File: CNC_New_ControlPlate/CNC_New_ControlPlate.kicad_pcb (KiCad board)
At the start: 2 copper layers, 152 x 73 mm, 38 parts, among them J1 OTHER, J2 Conn_01x02, J3 STEPPERS, J4 SPINDEL, U1 PC847, U2 PC847, U3 7406, U4 ATtiny2313V-10P, Y1 4MHz

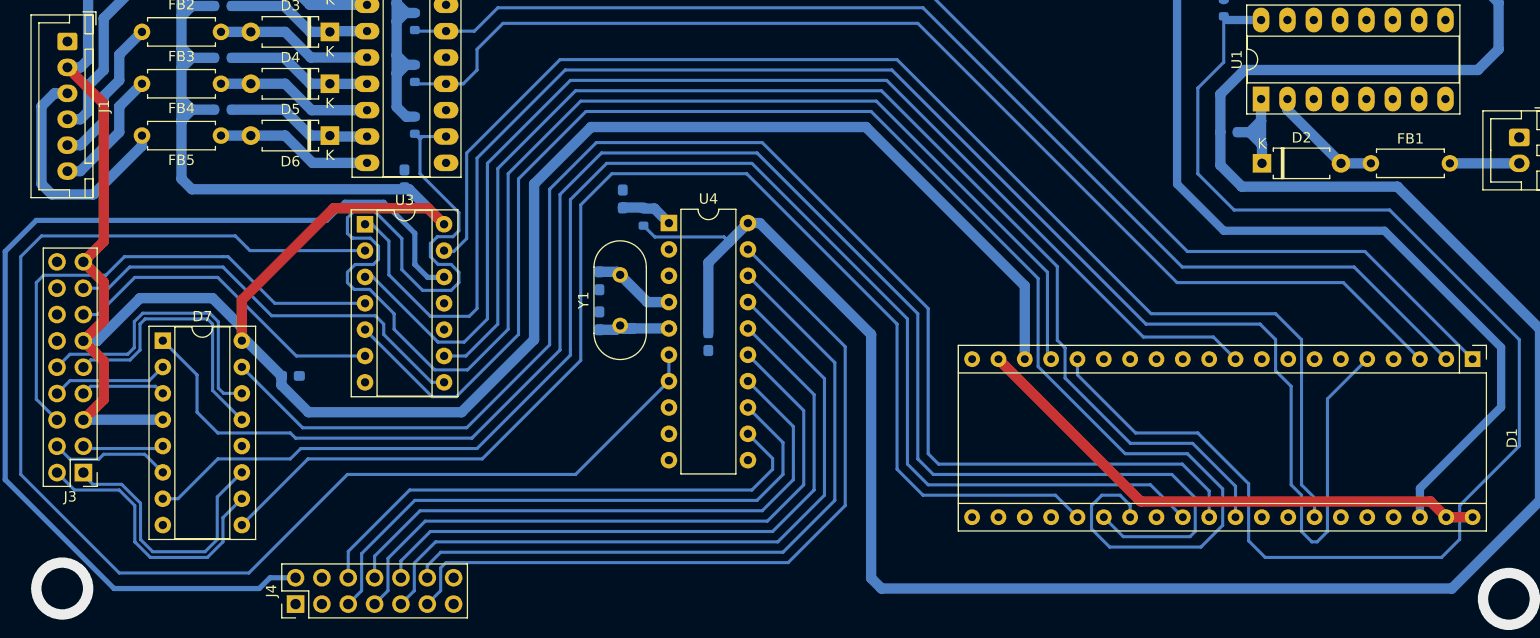
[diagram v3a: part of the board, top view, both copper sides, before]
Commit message: Edit PCB, add jumpers
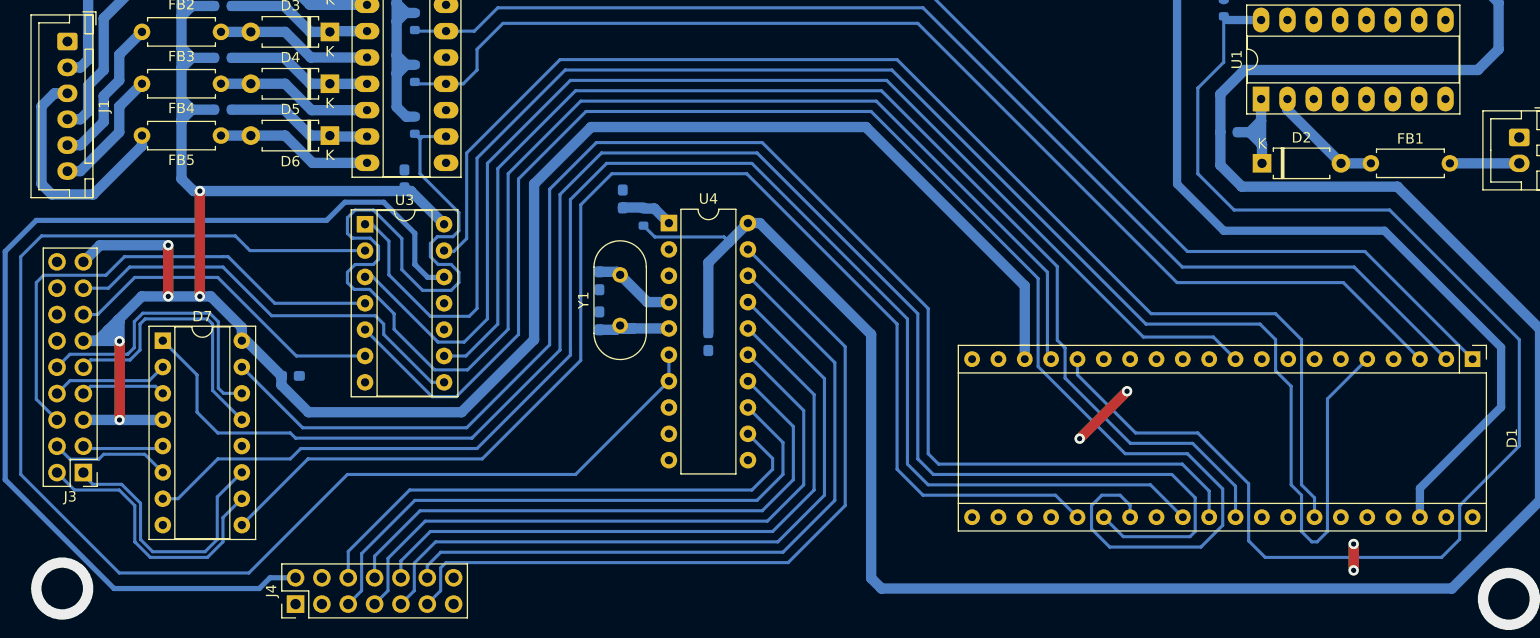
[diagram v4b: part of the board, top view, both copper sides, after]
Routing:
- net GNDREF: track 52.6 -> 9.55 mm, vias 4 -> 8
- net +5V: track 655.5 -> 627.6 mm, vias 0 -> 6

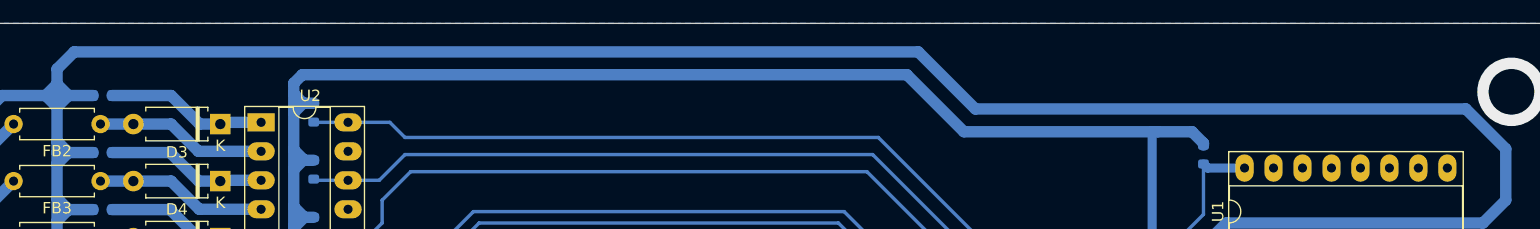
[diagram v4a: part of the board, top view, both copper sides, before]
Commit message: [+] Добавлен разъем питания
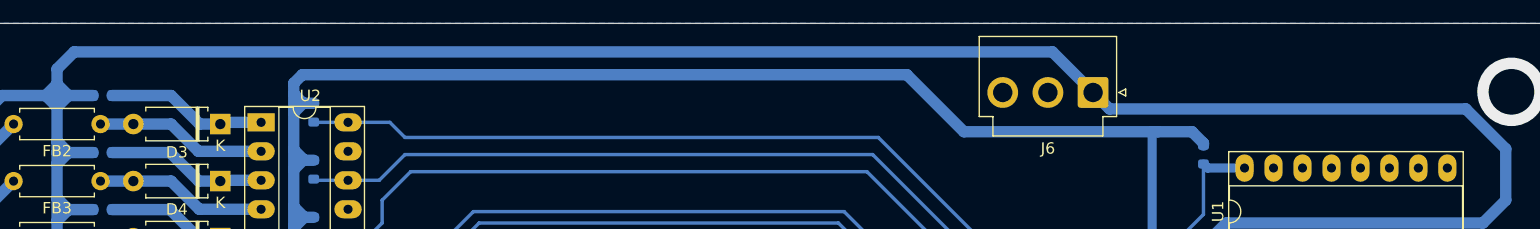
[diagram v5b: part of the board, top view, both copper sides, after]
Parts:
- added J6: Conn_01x03, Connector_JST:JST_VH_B3P-VH_1x03_P3.96mm_Vertical, F.Cu at (169.8, 83.1)
